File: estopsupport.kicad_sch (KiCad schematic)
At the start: 24 parts, among them J1 PWR, J2 CONTACTOR, J3 ESTOP2, J4 ESTOP1, J5 TAP_ESTOP, J6 5V_IN, U1 PC817, U2 BTS6163D

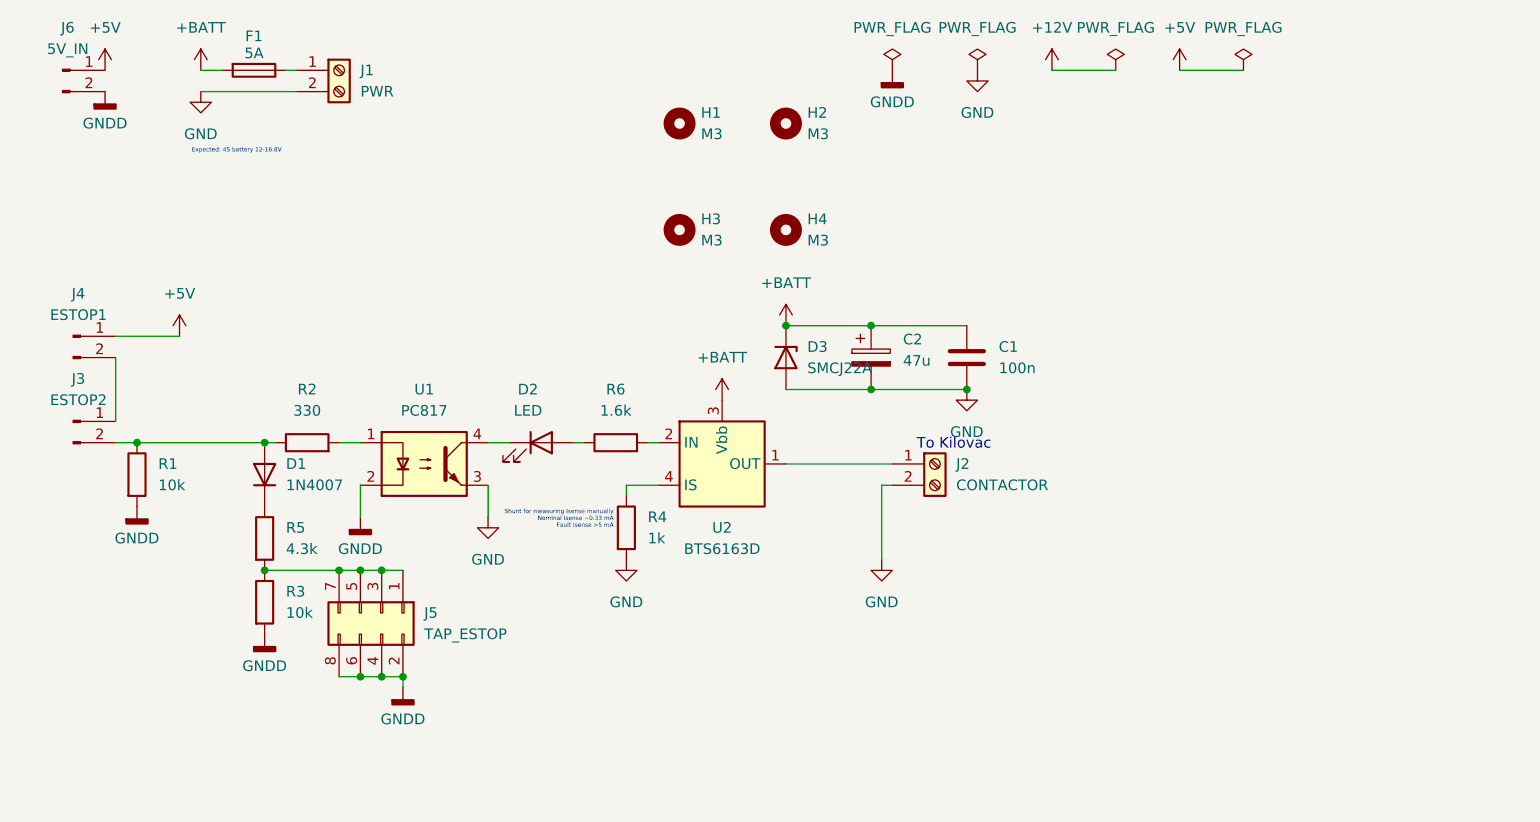
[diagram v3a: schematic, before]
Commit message: updated pcb to accomodate relay
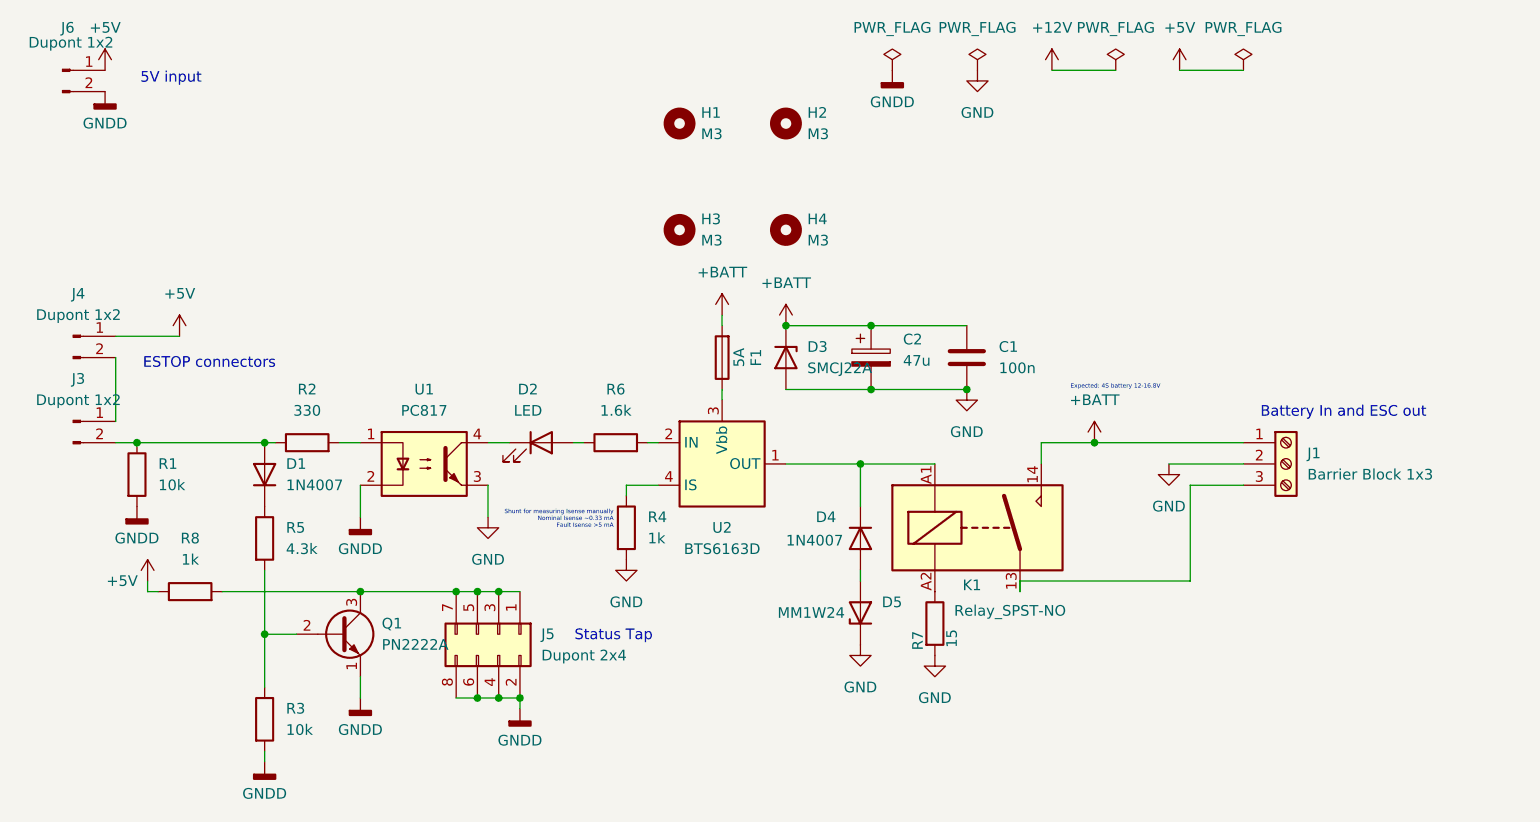
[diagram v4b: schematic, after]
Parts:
- removed J2: CONTACTOR, TerminalBlock_Phoenix:TerminalBlock_Phoenix_MKDS-1,5-2_1x02_P5.00mm_Horizontal, symbol Connector:Screw_Terminal_01x02
- added D4: 1N4007, Diode_SMD:D_SMA, symbol Device:D
- added D5: MM1W24, Diode_SMD:D_SOD-123, symbol Device:D_Zener
- added K1: Relay_SPST-NO, EasyEDA_Lib:RELAY-TH_JQX-V7H-012-1HP, symbol Relay:Relay_SPST-NO
- added Q1: PN2222A, Package_TO_SOT_THT:TO-92_Inline, symbol Transistor_BJT:PN2222A
- added R7: 15, Resistor_SMD:R_0603_1608Metric, symbol Device:R
- added R8: 1k, Resistor_SMD:R_0603_1608Metric, symbol Device:R
- J1: value PWR -> Barrier Block 1x3; footprint TerminalBlock_Phoenix:TerminalBlock_Phoenix_MKDS-1,5-2_1x02_P5.00mm_Horizontal -> EasyEDA_Lib:CONN-TH_KF88SA-16.0-3P; symbol Connector:Screw_Terminal_01x02 -> Connector:Screw_Terminal_01x03
- J3: value ESTOP2 -> Dupont 1x2
- J4: value ESTOP1 -> Dupont 1x2
- J5: value TAP_ESTOP -> Dupont 2x4
- J6: value 5V_IN -> Dupont 1x2
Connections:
- net +5V: now also R8.1
- net +BATT: now also J1.1 (Pin_1), K1.14; no longer U2.3 (Vbb)
- net GND: now also D5.1 (K), R7.2
- net GNDD: now also Q1.1 (E)
- net at F1.1: now also U2.3 (Vbb); no longer J1.1 (Pin_1)
- net at U2.1 (OUT), U2.5 (OUT): now also D4.1 (K), K1.A1
- net at J5.1 (Pin_1), J5.3 (Pin_3), J5.5 (Pin_5)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: now also Q1.3 (C), R8.2; no longer R3.1, R5.2
- new net: K1.A2, R7.1
- new net: D4.2 (A), D5.2 (A)
- new net: J1.3 (Pin_3), K1.13
- new net: Q1.2 (B), R3.1, R5.2
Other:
- note added: "5V input"
- note added: "Battery In and ESC out"
- note added: "ESTOP connectors"
- note added: "Status Tap"
- note removed: "To Kilovac"
- moved on the sheet: J5, R3

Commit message: minor fixes and updates
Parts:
- R7: footprint Resistor_SMD:R_0603_1608Metric -> Resistor_SMD:R_1812_4532Metric
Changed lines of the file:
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@@
 			)
 		)
-		(property "Footprint" "Resistor_SMD:R_0603_1608Metric"
+		(property "Footprint" "Resistor_SMD:R_1812_4532Metric"
 			(at 117.602 85.09 90)
 			(hide yes)

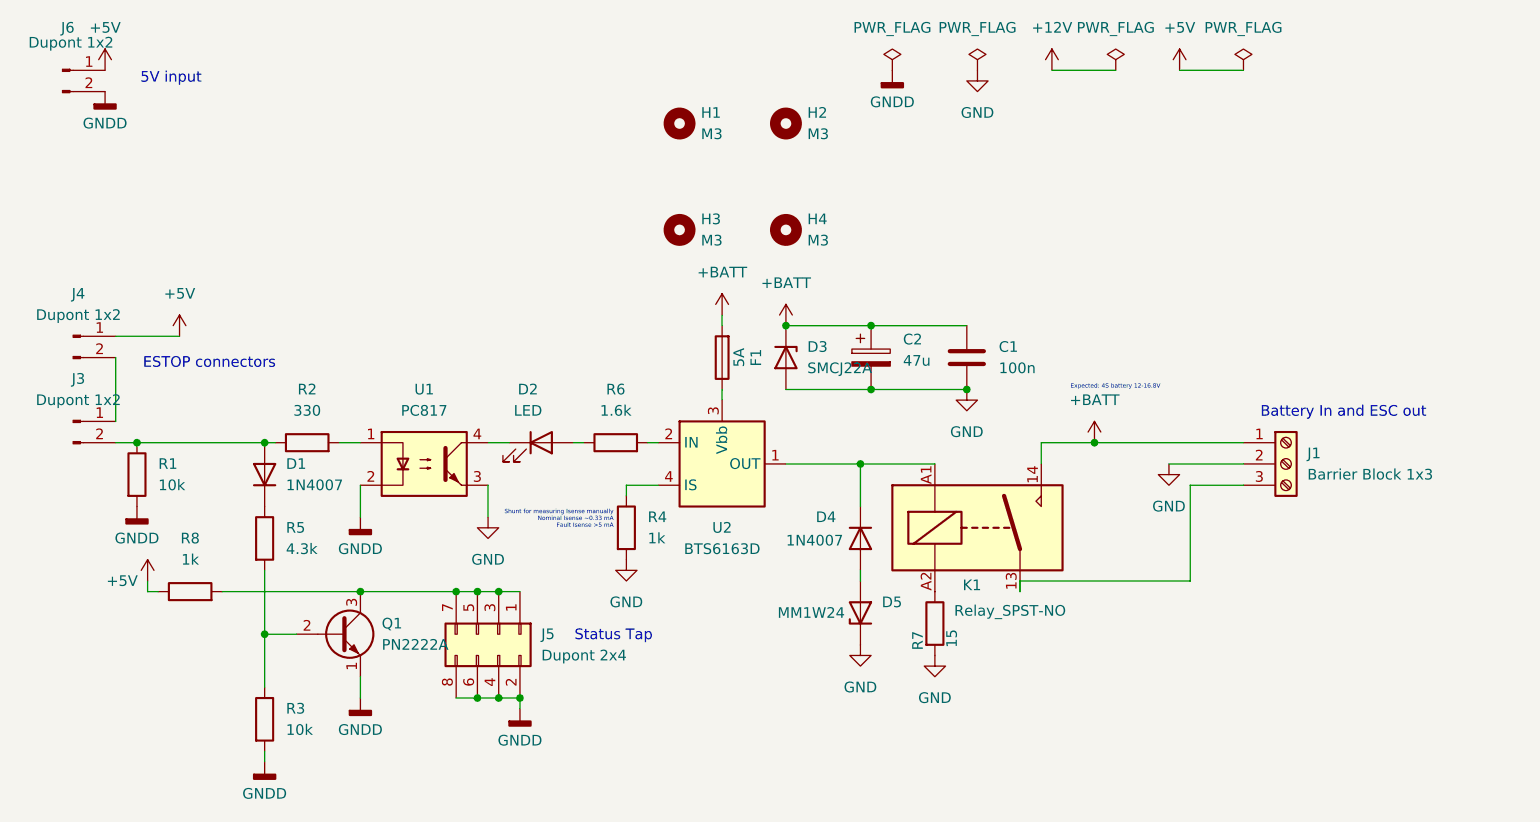
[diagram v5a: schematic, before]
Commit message: feat: simplified circuit with 2n7004 mosfet, routed power side - awaiting gpio capability confirmation
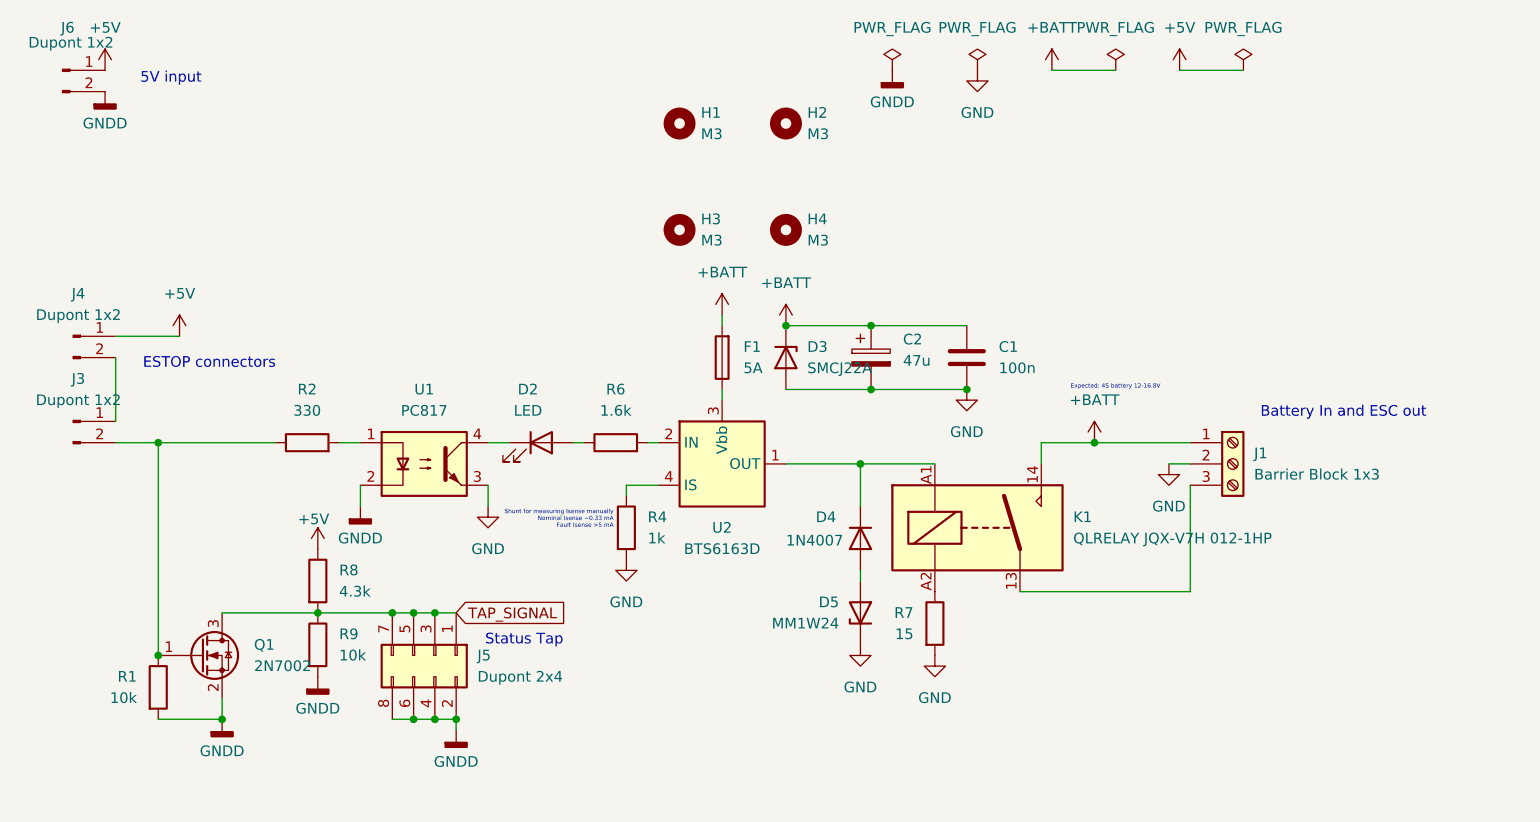
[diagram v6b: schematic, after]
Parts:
- removed D1: 1N4007, Diode_SMD:D_SMA, symbol Device:D
- removed R3: 10k, Resistor_SMD:R_0603_1608Metric, symbol Device:R
- removed R5: 4.3k, Resistor_SMD:R_0603_1608Metric, symbol Device:R
- added R9: 10k, Resistor_SMD:R_0603_1608Metric, symbol Device:R
- J5: footprint Connector_PinSocket_2.54mm:PinSocket_2x04_P2.54mm_Horizontal -> Connector_PinSocket_2.54mm:PinSocket_2x04_P2.54mm_Vertical
- K1: value Relay_SPST-NO -> QLRELAY JQX-V7H 012-1HP; footprint EasyEDA_Lib:RELAY-TH_JQX-V7H-012-1HP -> easyeda-modified:RELAY-TH_JQX-V7H-012-1HP
- Q1: value PN2222A -> 2N7002; footprint Package_TO_SOT_THT:TO-92_Inline -> Package_TO_SOT_SMD:SOT-23; symbol Transistor_BJT:PN2222A -> Transistor_FET:2N7002
- R8: value 1k -> 4.3k
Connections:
- net GNDD: now also Q1.2 (S), R9.2; no longer Q1.1 (E)
- net TAP_SIGNAL: now reaches J5.1 (Pin_1), J5.3 (Pin_3), J5.5 (Pin_5), J5.7 (Pin_7), Q1.3 (D), R8.2
- net TAP_SIGNAL: now also R9.1
- net at J3.2 (Pin_2), R1.1, R2.1: now also Q1.1 (G)
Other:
- moved on the sheet: J1, J5, R1, R8

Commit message: chore: geographical reannotate
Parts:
- renumbered D4 to D1, D5 to D2, D2 to D4, J3 to J2, J4 to J3, J6 to J4, R7 to R1, R1 to R2, R2 to R3, R6 to R4, R8 to R5, R9 to R6, R4 to R7, U2 to U1, U1 to U2
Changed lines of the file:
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@@
 		(dnp no)
 		(fields_autoplaced yes)
-		(property "Reference" "R7"
+		(property "Reference" "R1"
 			(at 116.84 83.8199 0)
 			(show_name no)
@@
 			(project "estopsupport"
 				(path "/ca51e45a-2cf8-42c4-bf53-5bd38d2544be"
-					(reference "R7")
+					(reference "R1")
 					(unit 1)
 				)
@@
 		(dnp no)
 		(fields_autoplaced yes)
-		(property "Reference" "D5"
+		(property "Reference" "D2"
 			(at 107.95 82.5499 90)
 			(show_name no)
@@
 			(project "estopsupport"
 				(path "/ca51e45a-2cf8-42c4-bf53-5bd38d2544be"
-					(reference "D5")
+					(reference "D2")
 					(unit 1)
 				)
@@
 		(dnp no)
 		(fields_autoplaced yes)
-		(property "Reference" "U2"
+		(property "Reference" "U1"
 			(at 93.98 73.66 0)
 			(show_name no)
@@
 			(project "estopsupport"
 				(path "/ca51e45a-2cf8-42c4-bf53-5bd38d2544be"
-					(reference "U2")
+					(reference "U1")
 					(unit 1)
 				)
@@
 		(dnp no)
 		(fields_autoplaced yes)
-		(property "Reference" "R9"
+		(property "Reference" "R6"
 			(at 48.26 86.3599 0)
 			(show_name no)
@@
 			(project "estopsupport"
 				(path "/ca51e45a-2cf8-42c4-bf53-5bd38d2544be"
-					(reference "R9")
+					(reference "R6")
 					(unit 1)
 				)
@@
 		(dnp no)
 		(fields_autoplaced yes)
-		(property "Reference" "R8"
+		(property "Reference" "R5"
 			(at 48.26 78.7399 0)
 			(show_name no)
@@
 			(project "estopsupport"
 				(path "/ca51e45a-2cf8-42c4-bf53-5bd38d2544be"
-					(reference "R8")
+					(reference "R5")
 					(unit 1)
 				)
@@
 		(dnp no)
 		(fields_autoplaced yes)
-		(property "Reference" "R1"
+		(property "Reference" "R2"
 			(at 24.13 91.4399 0)
 			(show_name no)
@@
 			(project "estopsupport"
 				(path "/ca51e45a-2cf8-42c4-bf53-5bd38d2544be"
-					(reference "R1")
+					(reference "R2")
 					(unit 1)
 				)
@@
 		(dnp no)
 		(fields_autoplaced yes)
-		(property "Reference" "U1"
+		(property "Reference" "U2"
 			(at 58.42 57.15 0)
 			(show_name no)
@@
 			(project "estopsupport"
 				(path "/ca51e45a-2cf8-42c4-bf53-5bd38d2544be"
-					(reference "U1")
+					(reference "U2")
 					(unit 1)
 				)
@@
 		(dnp no)
 		(fields_autoplaced yes)
-		(property "Reference" "J3"
+		(property "Reference" "J2"
 			(at 17.145 55.88 0)
 			(show_name no)
@@
 			(project "estopsupport"
 				(path "/ca51e45a-2cf8-42c4-bf53-5bd38d2544be"
-					(reference "J3")
+					(reference "J2")
 					(unit 1)
 				)
@@
 		(dnp no)
 		(fields_autoplaced yes)
-		(property "Reference" "R6"
+		(property "Reference" "R4"
 			(at 81.28 57.15 90)
 			(show_name no)
@@
 			(project "estopsupport"
 				(path "/ca51e45a-2cf8-42c4-bf53-5bd38d2544be"
-					(reference "R6")
+					(reference "R4")
 					(unit 1)
 				)
@@
 		(dnp no)
 		(fields_autoplaced yes)
-		(property "Reference" "D2"
+		(property "Reference" "D4"
 			(at 70.8025 57.15 0)
 			(show_name no)
@@
 			(project "estopsupport"
 				(path "/ca51e45a-2cf8-42c4-bf53-5bd38d2544be"
-					(reference "D2")
+					(reference "D4")
 					(unit 1)
 				)
@@
 		(in_pos_files yes)
 		(dnp no)
-		(property "Reference" "J6"
+		(property "Reference" "J4"
 			(at 15.875 13.97 0)
 			(show_name no)
@@
 			(project "estopsupport"
 				(path "/ca51e45a-2cf8-42c4-bf53-5bd38d2544be"
-					(reference "J6")
+					(reference "J4")
 					(unit 1)
 				)
@@
 		(dnp no)
 		(fields_autoplaced yes)
-		(property "Reference" "J4"
+		(property "Reference" "J3"
 			(at 17.145 45.72 0)
 			(show_name no)
@@
 			(project "estopsupport"
 				(path "/ca51e45a-2cf8-42c4-bf53-5bd38d2544be"
-					(reference "J4")
+					(reference "J3")
 					(unit 1)
 				)
@@
 		(dnp no)
 		(fields_autoplaced yes)
-		(property "Reference" "R4"
+		(property "Reference" "R7"
 			(at 85.09 72.3899 0)
 			(show_name no)
@@
 			(project "estopsupport"
 				(path "/ca51e45a-2cf8-42c4-bf53-5bd38d2544be"
-					(reference "R4")
+					(reference "R7")
 					(unit 1)
 				)
@@
 		(in_pos_files yes)
 		(dnp no)
-		(property "Reference" "D4"
+		(property "Reference" "D1"
 			(at 105.156 72.39 90)
 			(show_name no)
@@
 			(project "estopsupport"
 				(path "/ca51e45a-2cf8-42c4-bf53-5bd38d2544be"
-					(reference "D4")
+					(reference "D1")
 					(unit 1)
 				)
@@
 		(dnp no)
 		(fields_autoplaced yes)
-		(property "Reference" "R2"
+		(property "Reference" "R3"
 			(at 44.45 57.15 90)
 			(show_name no)
@@
 			(project "estopsupport"
 				(path "/ca51e45a-2cf8-42c4-bf53-5bd38d2544be"
-					(reference "R2")
+					(reference "R3")
 					(unit 1)
 				)
